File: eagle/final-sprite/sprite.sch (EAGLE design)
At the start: 60 parts, among them P1 SPRITE_PIN, P2 SPRITE_PIN, U1 CC430F5137, U2 DRV8833CRTER, U3 DRV8833CRTER, X1 TCXO_7Z

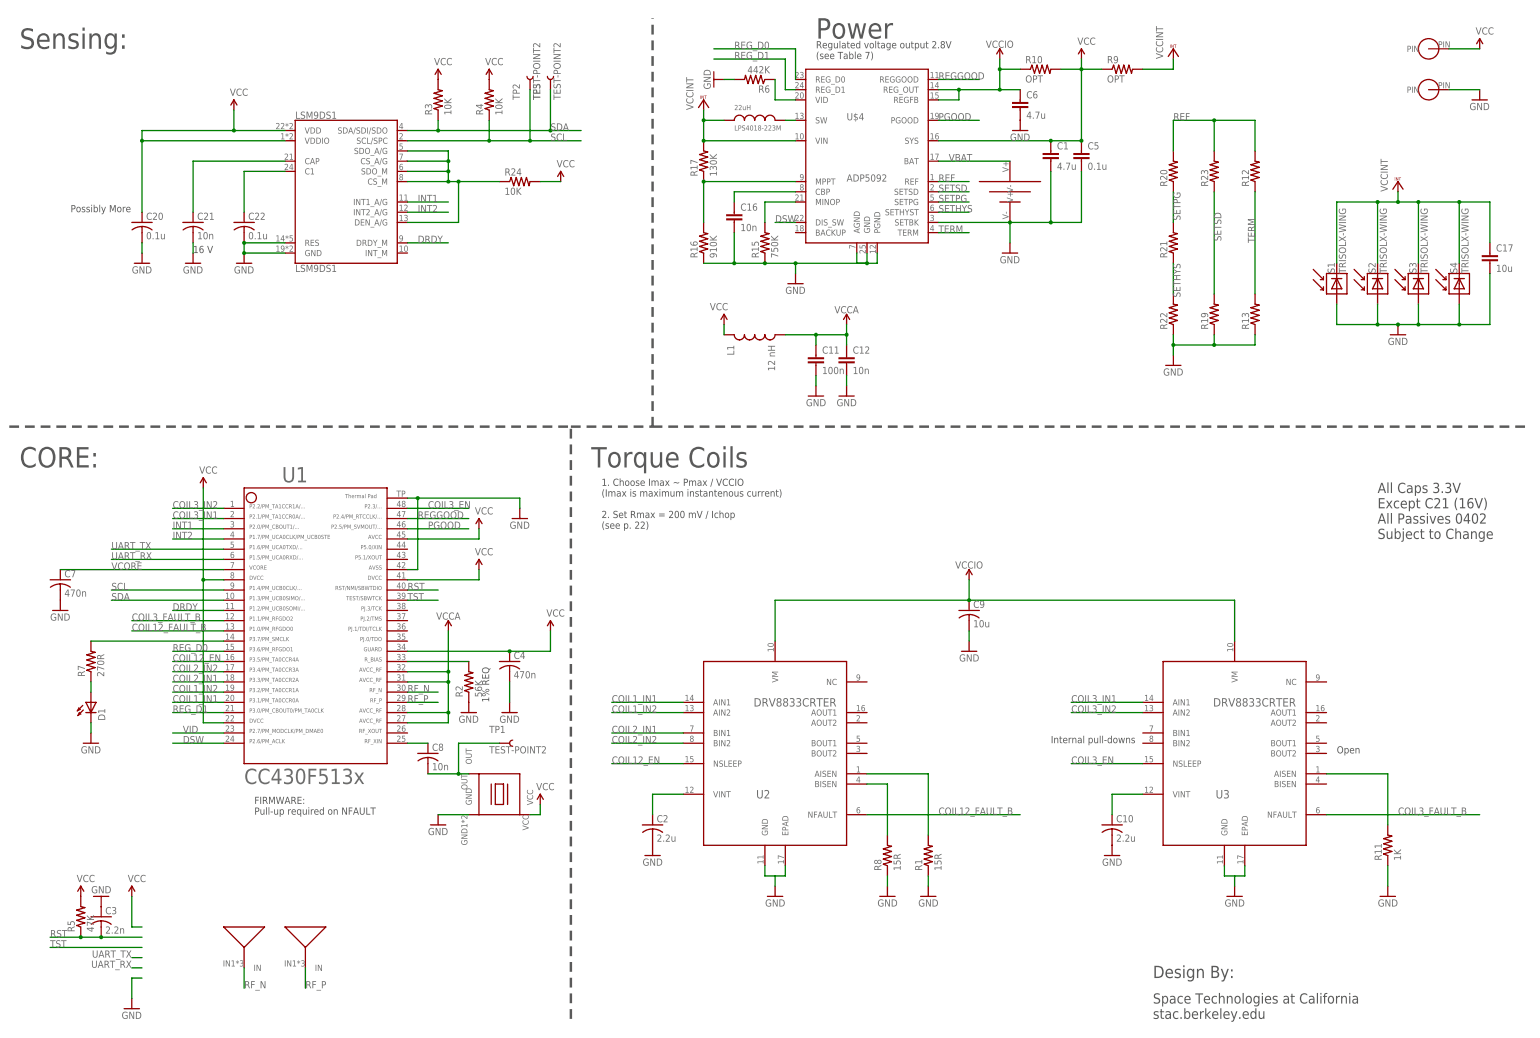
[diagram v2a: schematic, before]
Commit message: Updated schematic with DRV8837 drivers
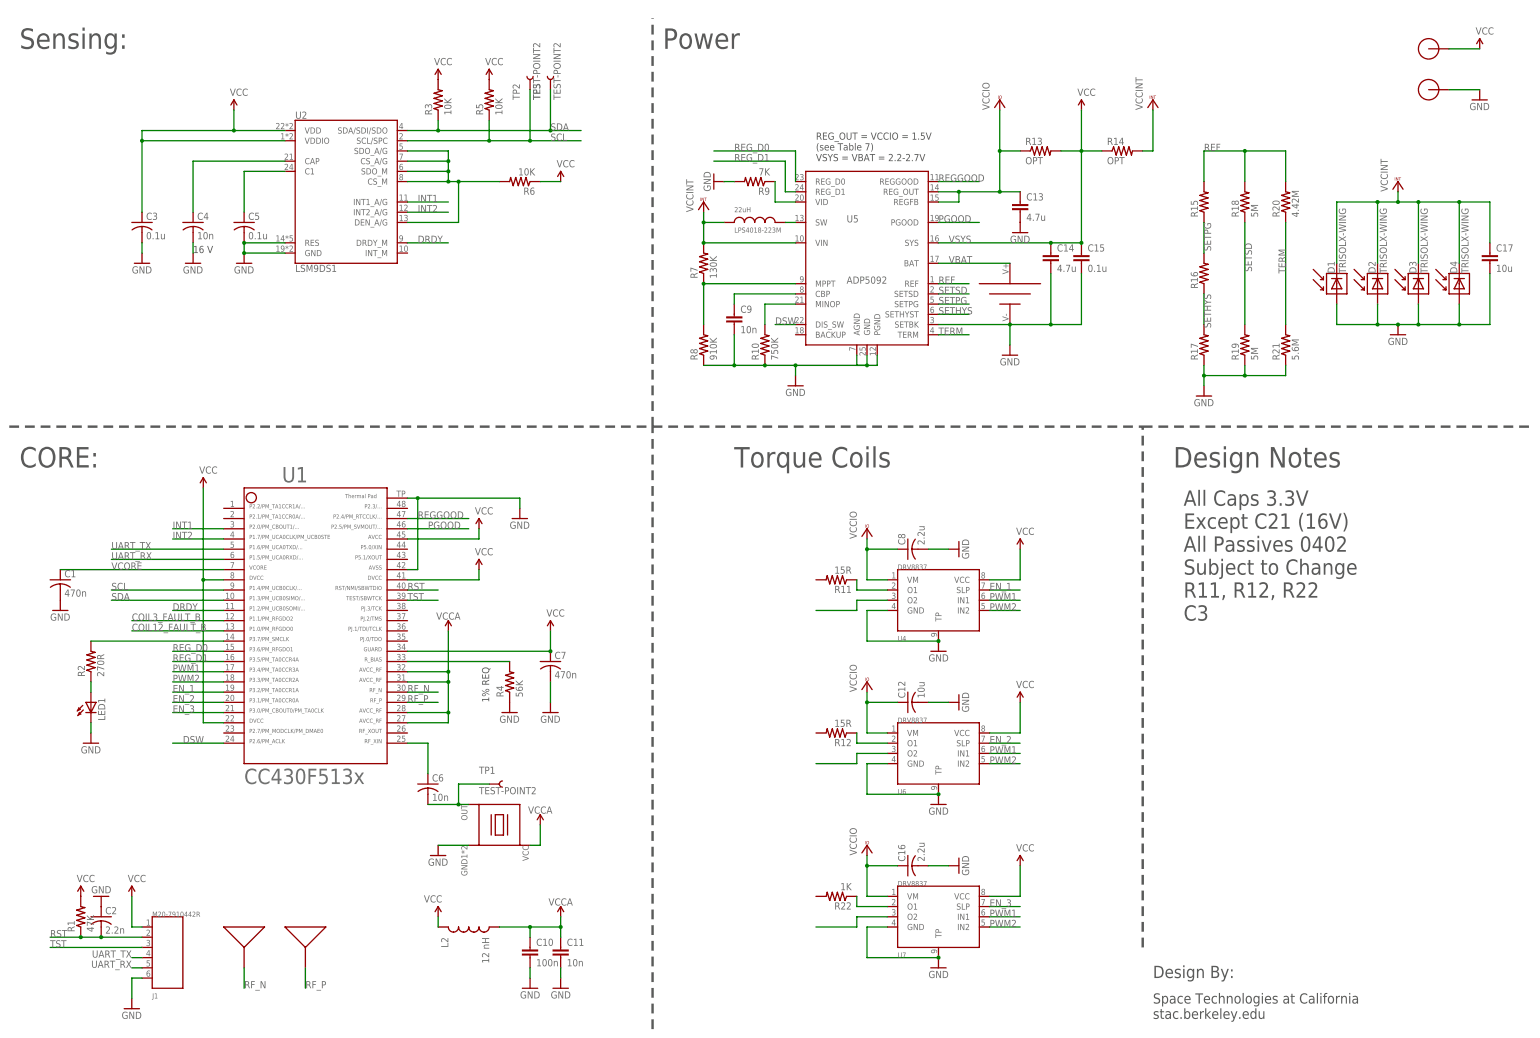
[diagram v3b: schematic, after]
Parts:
- removed ANT-N, ANT-P: ANTENNA, SpriteAntenna:ANTENNA
- removed C20, C22: 0.1u, rcl:C-USC0402
- removed C21: 10n, rcl:C-USC0402
- removed LSM9DS1: LSM9DS1, SparkFun-Sensors:LSM9DS1
- removed P1, P2: SPRITE_PIN, SpritePin:SPRITE_PIN
- removed R23: (no value), resistor:R-US_R0402
- removed R24: 10K, rcl:R-US_R0402
- removed S1, S2, S3, S4: TRISOLX-WING, TriSolX_QzQube:TRISOLX-WING
- removed U$1: UMAC, UMAC:UMAC
- removed U$4: ADP5092, STAC:ADP5092
- removed U$5: LPS4018-223M, STAC:LPS4018-223M
- added A1, A2: SPRITEANTENNA_ANTENNA, STAC:SPRITEANTENNA_ANTENNA
- added B1: UMAC_UMAC, STAC:UMAC_UMAC
- added C13, C14: 4.7u, resistor:C-EUC0402
- added C15: 0.1u, resistor:C-EUC0402
- added D2, D3, D4: TRISOLX-WING, STAC:TRISOLX-WING
- added J1: M20-7910442R, STAC:M20-7910442R
- added L2: 12 nH, SparkFun:INDUCTOR0603
- added LED1: (no value), SparkFun:LED0603
- added R14: OPT, resistor:R-US_R0402
- added R18: 5M, resistor:R-US_R0402
- added U4, U6, U7: DRV8837, STAC:DRV8837
- added U5: ADP5092, STAC:ADP5092
- added X2: SPRITEPIN_SPRITE_PIN, STAC:SPRITEPIN_SPRITE_PIN
- C1: value 4.7u -> 470n; device resistor:C-EUC0402 -> rcl:C-USC0402
- C10: value 2.2u -> 100n; device rcl:C-USC0402 -> resistor:C-EUC0402
- C11: value 100n -> 10n
- C12: value 10n -> 10u; device resistor:C-EUC0402 -> rcl:C-USC0402
- C16: value 10n -> 2.2u; device resistor:C-EUC0402 -> rcl:C-USC0402
- C2: value 2.2u -> 2.2n
- C3: value 2.2n -> 0.1u
- C4: value 470n -> 10n
- C5: device resistor:C-EUC0402 -> rcl:C-USC0402
- C6: value 4.7u -> 10n; device resistor:C-EUC0402 -> rcl:C-USC0402
- C8: value 10n -> 2.2u
- C9: value 10u -> 10n; device rcl:C-USC0402 -> resistor:C-EUC0402
- D1: value (none) -> TRISOLX-WING; device SparkFun:LED0603 -> STAC:TRISOLX-WING
- L1: value 12 nH -> LPS4018-223M; device SparkFun:INDUCTOR0603 -> STAC:LPS4018-223M
- R1: value 15R -> 47K
- R10: value OPT -> 750K
- R11: value 1K -> 15R
- R12: value (none) -> 15R; device resistor:R-US_R0402 -> rcl:R-US_R0402
- R13: value (none) -> OPT
- R15: value 750K -> (none)
- R16: value 910K -> (none)
- R17: value 130K -> (none)
- R19: value (none) -> 5M
- R2: value 56K -> 270R
- R20: value (none) -> 4.42M
- R21: value (none) -> 5.6M
- R22: value (none) -> 1K; device resistor:R-US_R0402 -> rcl:R-US_R0402
- R4: value 10K -> 56K
- R5: value 47K -> 10K
- R6: value 442K -> 10K; device resistor:R-US_R0402 -> rcl:R-US_R0402
- R7: value 270R -> 130K; device rcl:R-US_R0402 -> resistor:R-US_R0402
- R8: value 15R -> 910K; device rcl:R-US_R0402 -> resistor:R-US_R0402
- R9: value OPT -> 7K
- U1: value CC430F5137 -> CC430F513X; device TI_MSP430_v16:CC430F513X---RGZ48 -> STAC:CC430F513X
- U2: value DRV8833CRTER -> LSM9DS1; device STAC:DRV8833CRTER -> SparkFun-Sensors:LSM9DS1
- U3: value DRV8833CRTER -> (none); device STAC:DRV8833CRTER -> STAC:SPRITETCXO_TCXO_7Z
- X1: value TCXO_7Z -> SPRITEPIN_SPRITE_PIN; device SpriteTCXO:TCXO_7Z -> STAC:SPRITEPIN_SPRITE_PIN
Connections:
- removed net COIL12_EN: U1.16, U2.NSLEEP
- removed net COIL1_IN1: U1.20, U2.AIN1
- removed net COIL1_IN2: U1.19, U2.AIN2
- removed net COIL2_IN1: U1.18, U2.BIN1
- removed net COIL2_IN2: U1.17, U2.BIN2
- removed net COIL3_EN: U1.48, U3.NSLEEP
- removed net COIL3_IN1: U1.2, U3.AIN1
- removed net COIL3_IN2: U1.1, U3.AIN2
- removed net N$10: R1.2, U2.AISEN
- removed net N$15: R11.2, U3.AISEN
- removed net N$9: R8.2, U2.BISEN
- removed net VID: U1.23
- new net EN_1: U1.19, U4.SLP
- new net EN_2: U1.20, U6.SLP
- new net EN_3: U1.21, U7.SLP
- new net N$14: U4.O2
- new net N$26: R12.1, U6.O1
- new net N$27: U6.O2
- new net N$28: U7.O2
- new net PWM1: U1.17, U4.IN1, U6.IN1, U7.IN1
- new net PWM2: U1.18, U4.IN2, U6.IN2, U7.IN2
- new net VSYS: C14.1, C15.1, R13.2, R14.1, U5.SYS
- net COIL12_FAULT_B: no longer U2.NFAULT
- net COIL3_FAULT_B: no longer U3.NFAULT
- net DRDY: now also U2.DRDY_M; no longer LSM9DS1.DRDY_M
- net DSW: now also U5.DIS_SW; no longer U$4.DIS_SW
- net GND: now also B1.V-, C13.2, C14.2, C15.2, C2.1, C3.2, C8.2, D1.A, D2.A, D3.A, D4.A, J1.P$6, LED1.C, R10.1, R17.1, R21.1, R4.1, R9.2, U2.RES, U4.GND, U4.TP, U5.AGND, U5.GND, U5.PGND, U5.SETBK, U6.GND, U6.TP, U7.GND, U7.TP, X2.PIN; no longer C2.2, C20.2, C21.2, C22.2, C3.1, C6.2, D1.C, LSM9DS1.GND, LSM9DS1.RES, P2.PIN, R1.1, R11.1, R13.1, R15.1, R16.1, R2.1, R22.1, R6.2, S1.A, S2.A, S3.A, S4.A, U$1.V-, U$4.AGND, U$4.GND, U$4.PGND, U$4.SETBK, U2.EPAD, U3.EPAD, X1.GND
- net INT1: now also U2.INT1_A/G; no longer LSM9DS1.INT1_A/G
- net INT2: now also U2.INT2_A/G; no longer LSM9DS1.INT2_A/G
- net N$1: now also C6.1; no longer C8.1
- net N$11: now also LED1.A, R2.1; no longer D1.A, R7.1
- net N$12: now also C6.2, U3.OUT; no longer C8.2, X1.OUT
- net N$13: now also R22.1, U7.O1; no longer C10.1, U3.VINT
- net N$16: now also R9.1, U5.VID; no longer R24.1, R6.1, U$4.VID
- net N$18: now also R7.1, R8.2, U5.MPPT; no longer R16.2, R17.1, U$4.MPPT
- net N$2: now also R2.2; no longer R7.2
- net N$20: now also R10.2, U5.MINOP; no longer R15.2, U$4.MINOP
- net N$21: now also C9.1, U5.CBP; no longer C16.1, U$4.CBP
- net N$22: now also L1.P$2, U5.SW; no longer U$4.SW, U$5.P$2
- net N$3: now also R4.2; no longer R2.2
- net N$5: now also C5.1, U2.C1; no longer C22.1, LSM9DS1.C1
- net N$6: now also C4.1, U2.CAP; no longer C21.1, LSM9DS1.CAP
- net N$7: now also R6.2, U2.CS_A/G, U2.CS_M, U2.DEN_A/G, U2.SDO_A/G, U2.SDO_M; no longer LSM9DS1.CS_A/G, LSM9DS1.CS_M, LSM9DS1.DEN_A/G, LSM9DS1.SDO_A/G, LSM9DS1.SDO_M, R24.1
- net N$8: now also R11.1, U4.O1; no longer C2.1, U2.VINT
- net PGOOD: now also U5.PGOOD; no longer U$4.PGOOD
- net REF: now also R15.2, R18.2, U5.REF; no longer R12.2, R23.2, U$4.REF
- net REGGOOD: now also U5.REGGOOD; no longer U$4.REGGOOD
- net REG_D0: now also U5.REG_D0; no longer U$4.REG_D0
- net REG_D1: now also U1.16, U5.REG_D1; no longer U$4.REG_D1, U1.21
- net RF_N: now also A1.IN; no longer ANT-N.IN
- net RF_P: now also A2.IN; no longer ANT-P.IN
- net RST: now also C2.2, J1.P$2, R1.1; no longer C3.2, R5.1
- net SCL: now also R5.1, U2.SCL/SPC; no longer LSM9DS1.SCL/SPC, R4.1
- net SDA: now also U2.SDA/SDI/SDO; no longer LSM9DS1.SDA/SDI/SDO
- net SETHYS: now also R16.1, R17.2, U5.SETHYST; no longer R21.1, R22.2, U$4.SETHYST
- net SETPG: now also R15.1, R16.2, U5.SETPG; no longer R20.1, R21.2, U$4.SETPG
- net SETSD: now also R18.1, U5.SETSD; no longer R23.1, U$4.SETSD
- net TERM: now also R20.1, R21.2, U5.TERM; no longer R12.1, R13.2, U$4.TERM
- net TST: now also J1.P$3
- net UART_RX: now also J1.P$5
- net UART_TX: now also J1.P$4
- net VBAT: now also B1.V+, U5.BAT; no longer U$1.V+, U$4.BAT
- net VCC: now also C3.1, C7.1, J1.P$1, L2.1, R1.2, R6.1, U2.VDD, U2.VDDIO, U4.VCC, U6.VCC, U7.VCC, X1.PIN; no longer C1.1, C20.1, C4.1, C5.1, L1.1, LSM9DS1.VDD, LSM9DS1.VDDIO, P1.PIN, R10.2, R24.2, R4.2, R9.1, U$4.SYS, X1.VCC
- net VCCA: now also C10.1, L2.2, U3.VCC; no longer C12.1, L1.2
- net VCCINT: now also D1.C, D2.C, D3.C, D4.C, L1.P$1, R14.2, R7.2, U5.VIN; no longer R17.2, R9.2, S1.C, S2.C, S3.C, S4.C, U$4.VIN, U$5.P$1
- net VCCIO: now also C12.1, C13.1, C16.1, C8.1, R13.1, U4.VM, U5.REGFB, U5.REG_OUT, U6.VM, U7.VM; no longer C6.1, C9.1, R10.1, U$4.REGFB, U$4.REG_OUT, U2.VM, U3.VM
- net VCORE: now also C1.1; no longer C7.1
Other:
- note added: "All Caps 3.3V Except C21 (16V) All Passives 0402 Subject to Change R11, R12, R22 C3"
- note added: "Design Notes"
- note added: "REG_OUT = VCCIO = 1.5V (see Table 7) VSYS = VBAT = 2.2-2.7V"
- note removed: "1. Choose Imax ~ Pmax / VCCIO (Imax is maximum instantenous current) 2. Set Rmax = 200 mV / Ichop (see p. 22)"
- note removed: "All Caps 3.3V Except C21 (16V) All Passives 0402 Subject to Change"
- note removed: "FIRMWARE: Pull-up required on NFAULT"
- note removed: "Internal pull-downs"
- note removed: "Open"
- note removed: "Possibly More"
- note removed: "Regulated voltage output 2.8V (see Table 7)"
- moved on the sheet: C1, C10, C11, C12, C16, C2, C3, C4, C5, C6, C7, C8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

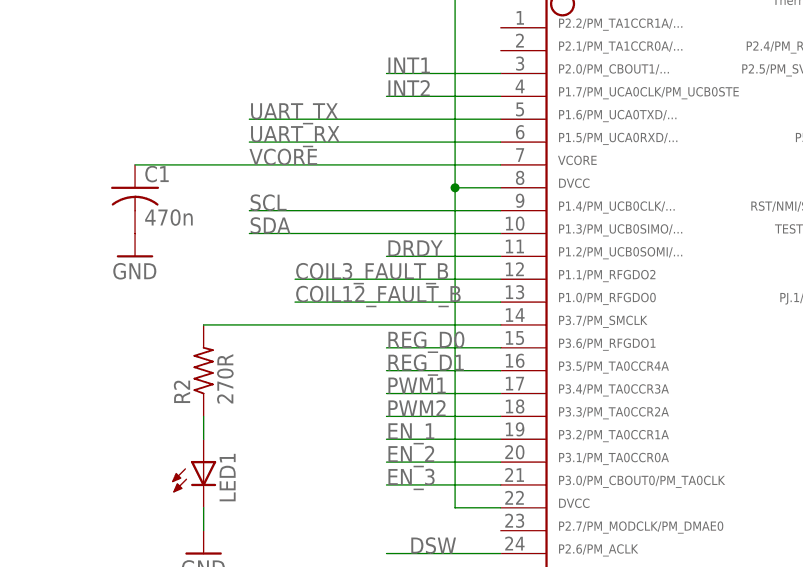
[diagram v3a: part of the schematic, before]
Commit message: Remove unused fault nets
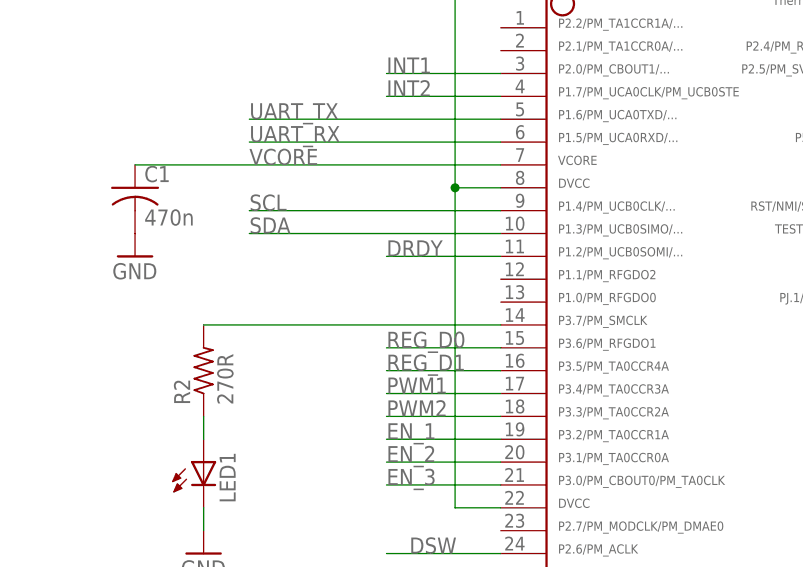
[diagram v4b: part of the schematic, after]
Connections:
- removed net COIL12_FAULT_B: U1.13
- removed net COIL3_FAULT_B: U1.12
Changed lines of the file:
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@@
 <?xml version="1.0" encoding="utf-8"?>
 <!DOCTYPE eagle SYSTEM "eagle.dtd">
-<eagle version="9.0.1">
+<eagle version="9.0.0">
 <drawing>
 <settings>
@@
 </segment>
 </net>
-<net name="COIL12_FAULT_B" class="0">
-<segment>
-<wire x1="-20.32" y1="-218.44" x2="-43.18" y2="-218.44" width="0.1524" layer="91"/>
-<label x="-43.18" y="-218.44" size="1.778" layer="95"/>
-<pinref part="U1" gate="G$1" pin="13"/>
-</segment>
-</net>
-<net name="COIL3_FAULT_B" class="0">
-<segment>
-<wire x1="-20.32" y1="-215.9" x2="-43.18" y2="-215.9" width="0.1524" layer="91"/>
-<label x="-43.18" y="-215.9" size="1.778" layer="95"/>
-<pinref part="U1" gate="G$1" pin="12"/>
-</segment>
-</net>
